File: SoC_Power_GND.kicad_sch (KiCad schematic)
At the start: 17 parts, among them U1 rv1126/rv1109

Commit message: updated LCSC selection of capacitors
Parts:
- C57: value 10uF X5R 4V -> 10uF X5R 10V; LCSC (none) -> C77000; Model (none) -> GRM155R61A106ME44D; Vendor (none) -> muRata(村田)
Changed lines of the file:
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@@
       (effects (font (size 1.27 1.27)) (justify left))
     )
-    (property "Value" "10uF X5R 4V" (at 222.25 138.43 90)
+    (property "Value" "10uF X5R 10V" (at 222.25 138.43 90)
       (effects (font (size 1.27 1.27)) (justify left))
     )
@@
     )
     (property "Datasheet" "~" (at 226.06 129.54 0)
+      (effects (font (size 1.27 1.27)) hide)
+    )
+    (property "Description" "容值: 10uF 精度: ±20% 额定电压: 10V 材质(温度系数): X5R 材质:X5R" (at 226.06 129.54 0)
+      (effects (font (size 1.27 1.27)) hide)
+    )
+    (property "LCSC" "C77000" (at 226.06 129.54 0)
+      (effects (font (size 1.27 1.27)) hide)
+    )
+    (property "Model" "GRM155R61A106ME44D" (at 226.06 129.54 0)
+      (effects (font (size 1.27 1.27)) hide)
+    )
+    (property "Vendor" "muRata(村田)" (at 226.06 129.54 0)
       (effects (font (size 1.27 1.27)) hide)
     )
@@
       (effects (font (size 1.27 1.27)) (justify left))
     )
-    (property "Value" "10uF X5R 4V" (at 142.24 138.43 90)
+    (property "Value" "10uF X5R 10V" (at 142.24 138.43 90)
       (effects (font (size 1.27 1.27)) (justify left))
     )
@@
     )
     (property "Datasheet" "~" (at 146.05 129.54 0)
+      (effects (font (size 1.27 1.27)) hide)
+    )
+    (property "Description" "容值: 10uF 精度: ±20% 额定电压: 10V 材质(温度系数): X5R 材质:X5R" (at 146.05 129.54 0)
+      (effects (font (size 1.27 1.27)) hide)
+    )
+    (property "LCSC" "C77000" (at 146.05 129.54 0)
+      (effects (font (size 1.27 1.27)) hide)
+    )
+    (property "Model" "GRM155R61A106ME44D" (at 146.05 129.54 0)
+      (effects (font (size 1.27 1.27)) hide)
+    )
+    (property "Vendor" "muRata(村田)" (at 146.05 129.54 0)
       (effects (font (size 1.27 1.27)) hide)
     )
@@
       (effects (font (size 1.27 1.27)) (justify left))
     )
-    (property "Value" "10uF X5R 4V" (at 158.75 180.34 90)
+    (property "Value" "10uF X5R 10V" (at 158.75 180.34 90)
       (effects (font (size 1.27 1.27)) (justify left))
     )
@@
     )
     (property "Datasheet" "~" (at 162.56 171.45 0)
+      (effects (font (size 1.27 1.27)) hide)
+    )
+    (property "Description" "容值: 10uF 精度: ±20% 额定电压: 10V 材质(温度系数): X5R 材质:X5R" (at 162.56 171.45 0)
+      (effects (font (size 1.27 1.27)) hide)
+    )
+    (property "LCSC" "C77000" (at 162.56 171.45 0)
+      (effects (font (size 1.27 1.27)) hide)
+    )
+    (property "Model" "GRM155R61A106ME44D" (at 162.56 171.45 0)
+      (effects (font (size 1.27 1.27)) hide)
+    )
+    (property "Vendor" "muRata(村田)" (at 162.56 171.45 0)
       (effects (font (size 1.27 1.27)) hide)
     )
@@
       (effects (font (size 1.27 1.27)) (justify left))
     )
-    (property "Value" "10uF X5R 4V" (at 142.24 180.34 90)
+    (property "Value" "10uF X5R 10V" (at 142.24 180.34 90)
       (effects (font (size 1.27 1.27)) (justify left))
     )
@@
       (effects (font (size 1.27 1.27)) hide)
     )
+    (property "Description" "容值: 10uF 精度: ±20% 额定电压: 10V 材质(温度系数): X5R 材质:X5R" (at 146.05 171.45 0)
+      (effects (font (size 1.27 1.27)) hide)
+    )
+    (property "LCSC" "C77000" (at 146.05 171.45 0)
+      (effects (font (size 1.27 1.27)) hide)
+    )
+    (property "Model" "GRM155R61A106ME44D" (at 146.05 171.45 0)
+      (effects (font (size 1.27 1.27)) hide)
+    )
+    (property "Vendor" "muRata(村田)" (at 146.05 171.45 0)
+      (effects (font (size 1.27 1.27)) hide)
+    )

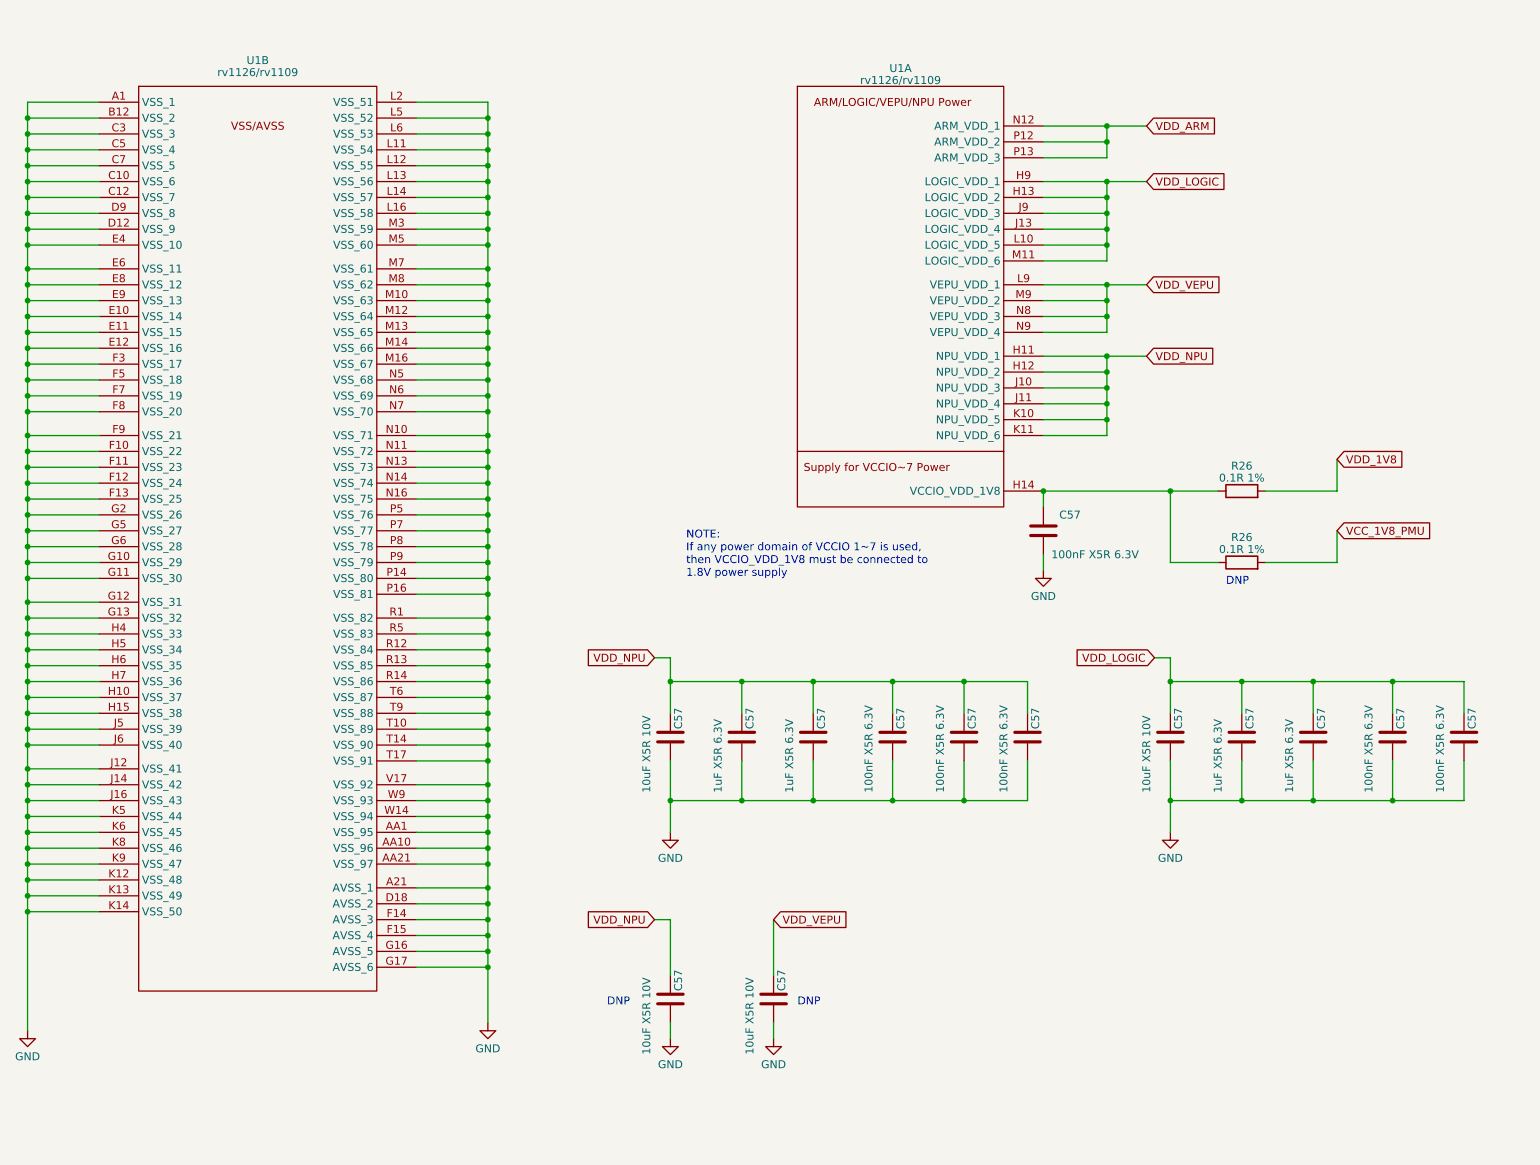
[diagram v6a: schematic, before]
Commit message: layout SoC Power and DDR capacitors
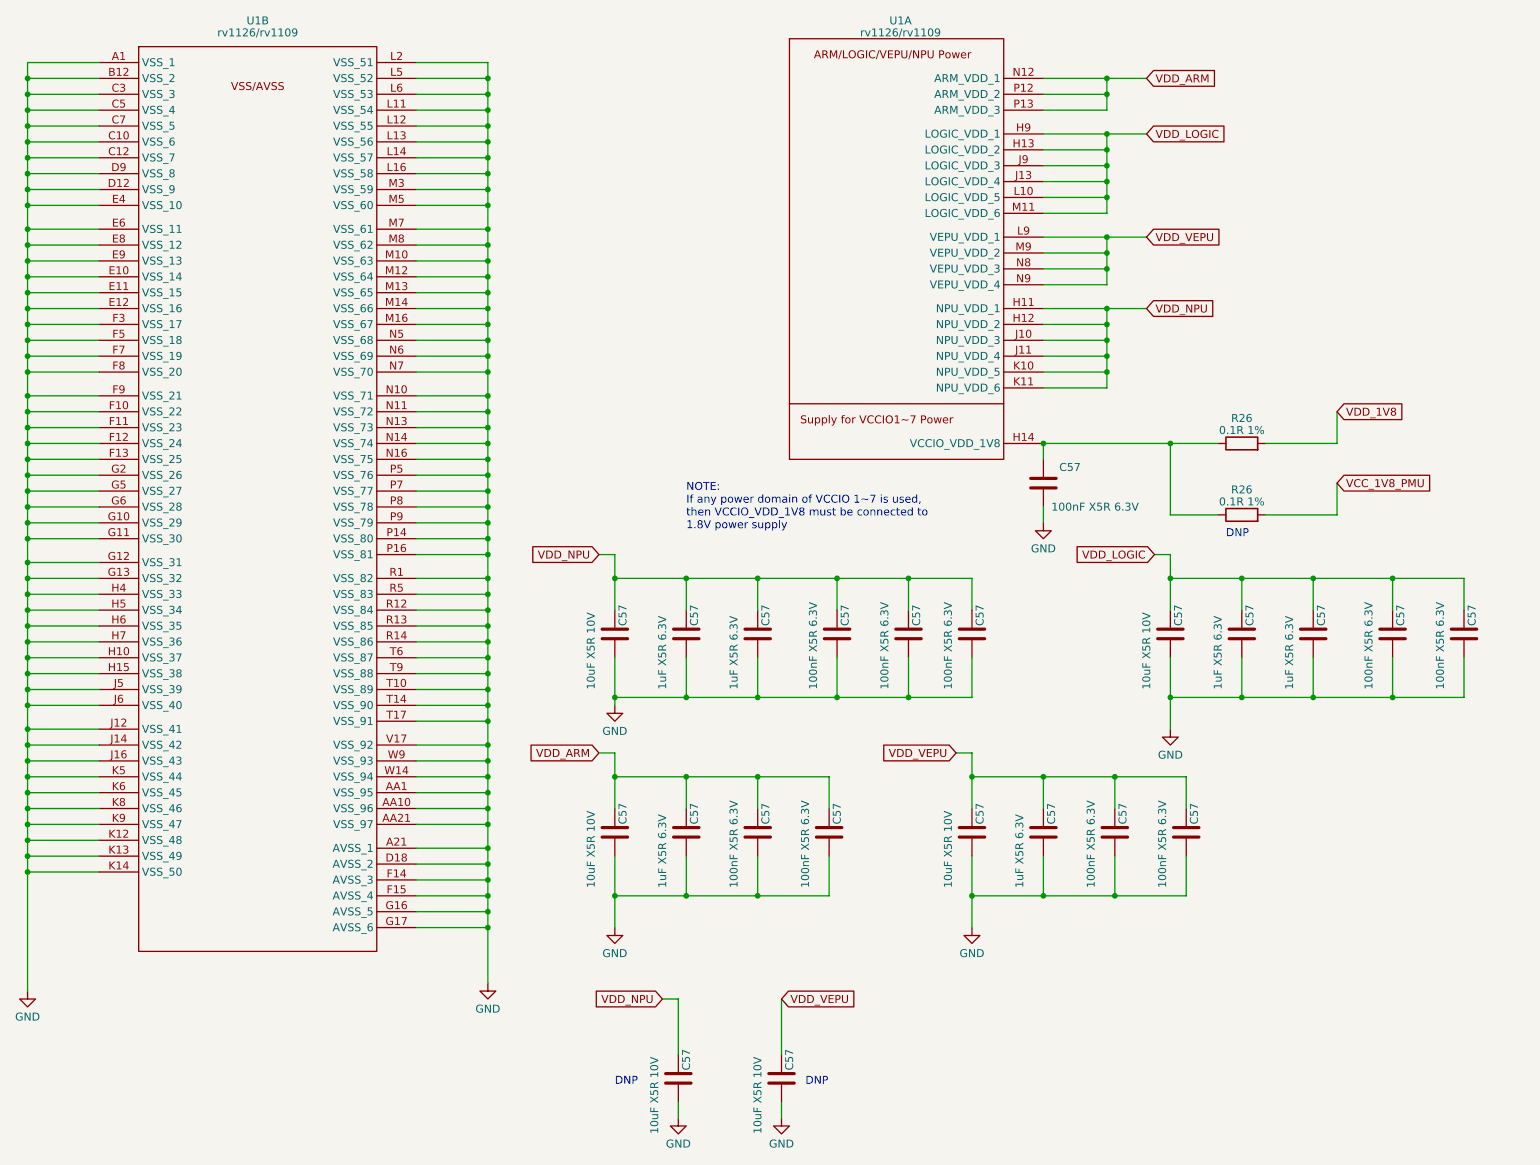
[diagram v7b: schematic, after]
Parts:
- added C57 (x2): 1uF X5R 6.3V, Capacitor_SMD:C_0402_1005Metric, symbol Device:C
- added C57 (x4): 100nF X5R 6.3V, Capacitor_SMD:C_0201_0603Metric, symbol Device:C
- added C57 (x2): 10uF X5R 10V, Capacitor_SMD:C_0402_1005Metric, symbol Device:C
- C57: LCSC C76934 -> C76928; Model GRM033R61A104KE15D -> GRM033R60J104KE19D
- C57: footprint Capacitor_SMD:C_0201_0603Metric -> Capacitor_SMD:C_0402_1005Metric; LCSC C76929 -> C15684; Model GRM033R60J105KEA2D -> GRM155R60J105KE19D
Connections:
- net GND: now also C57.2, C57.2, C57.2, C57.2, C57.2, C57.2, C57.2, C57.2
- net VDD_ARM: now also C57.1, C57.1, C57.1, C57.1
- net VDD_VEPU: now also C57.1, C57.1, C57.1, C57.1
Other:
- moved on the sheet: C57, R26, U1A, U1B
